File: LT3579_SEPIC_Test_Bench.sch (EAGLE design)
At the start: 159 parts

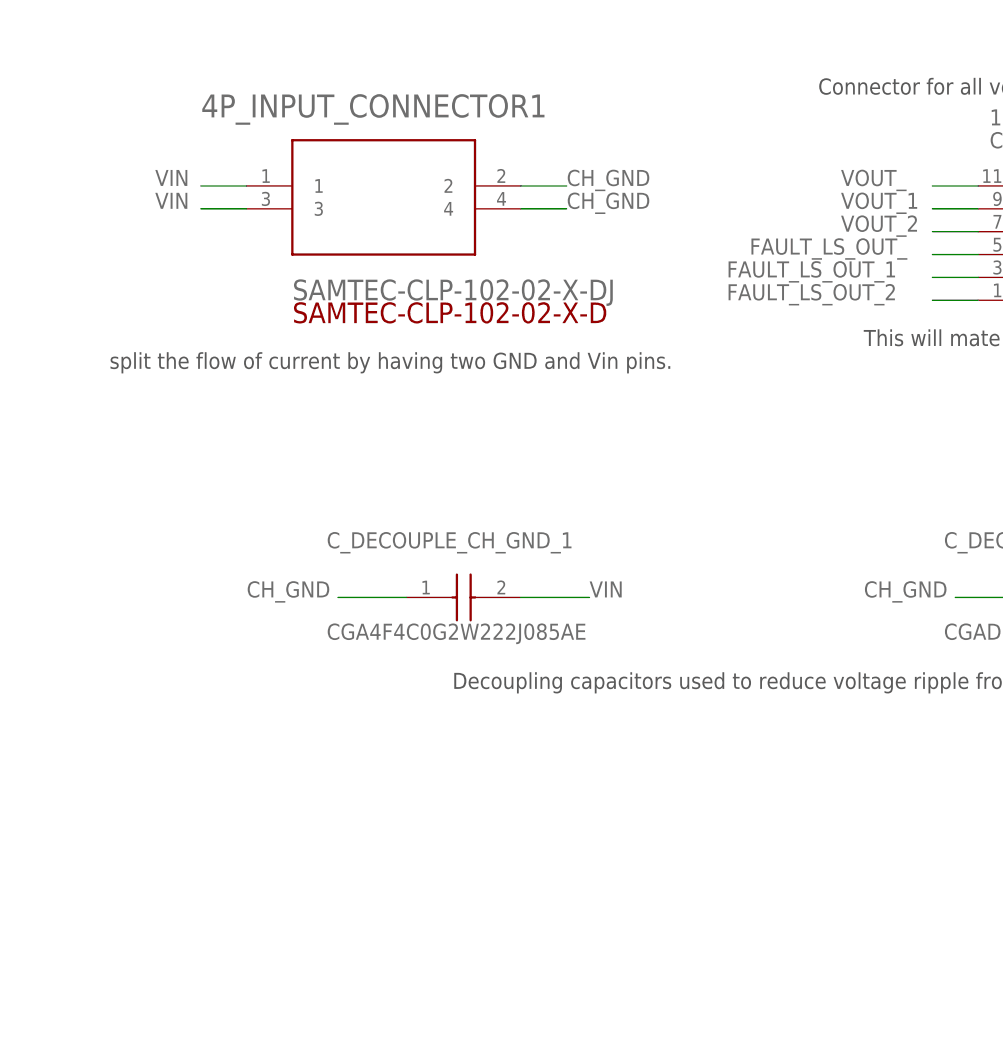
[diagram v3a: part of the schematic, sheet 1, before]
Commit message: Added Reverse Voltage Protection PMOS
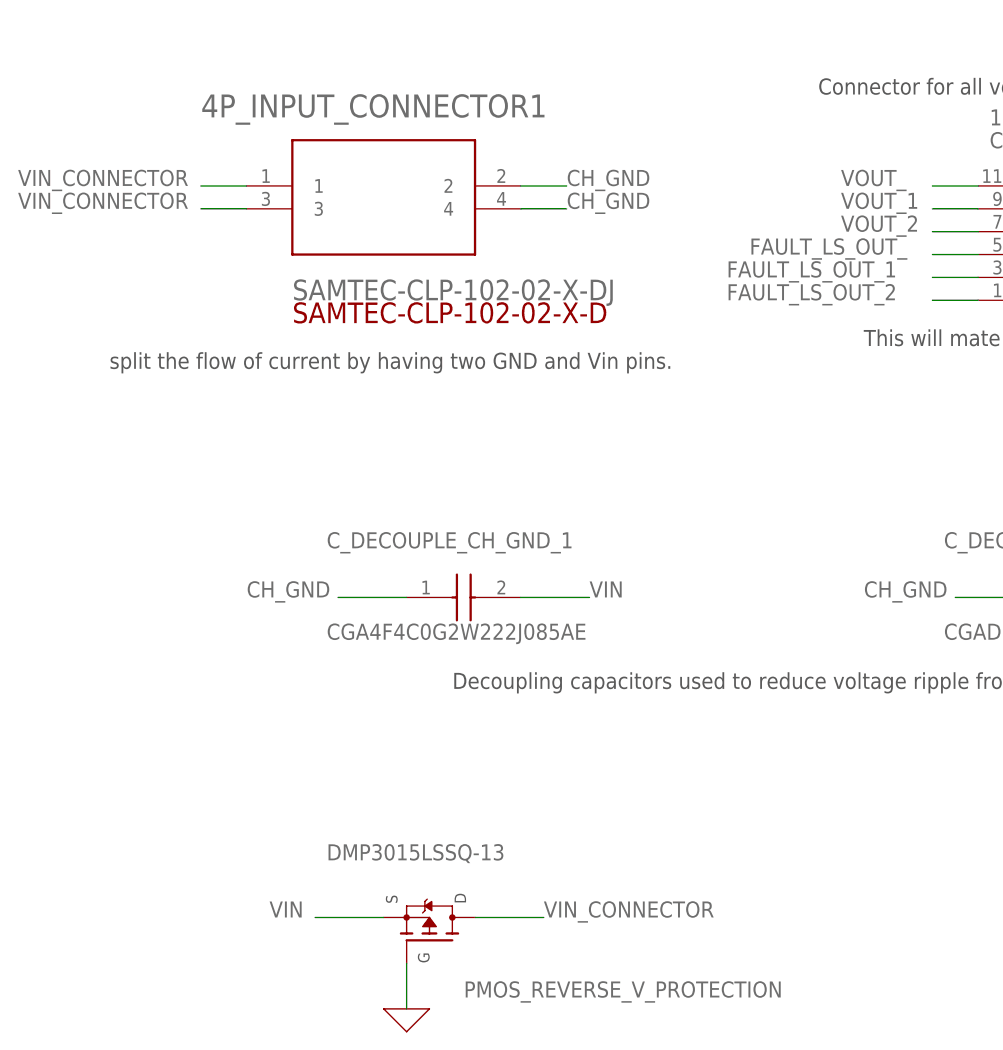
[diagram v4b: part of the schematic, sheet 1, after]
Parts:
- added PMOS_REVERSE_V_PROTECTION: DMP3015LSSQ-13, DMP3015LSSQ-13:DMP3015LSSQ-13
- D1_, D1_1, D1_2: value MBRS360T3G -> MBRS330T3G; device SamacSys_Parts:MBRS360T3G -> SamacSys_Parts:MBRS330T3G
- R_GATE_, R_GATE_1, R_GATE_2: value AC0805DR-0710KL -> AC0805FR-0710KL; device AC0805DR-0710KL:AC0805DR-0710KL -> SamacSys_Parts:AC0805FR-0710KL
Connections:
- new net VIN_CONNECTOR: 4P_INPUT_CONNECTOR1.1, 4P_INPUT_CONNECTOR1.3, PMOS_REVERSE_V_PROTECTION.D1
- net 0: now also PMOS_REVERSE_V_PROTECTION.G1
- net VIN: now also PMOS_REVERSE_V_PROTECTION.S1; no longer 4P_INPUT_CONNECTOR1.1, 4P_INPUT_CONNECTOR1.3
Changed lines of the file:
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@@
 <parts>
 <part name="LT3579_IC_" library="SamacSys_Parts" deviceset="LT3579EFE#PBF" device=""/>
-<part name="D1_" library="SamacSys_Parts" deviceset="MBRS360T3G" device=""/>
+<part name="D1_" library="SamacSys_Parts" deviceset="MBRS330T3G" device=""/>
 <part name="C_IN_1_" library="SamacSys_Parts" deviceset="CGA4J1X7R1E475K125AE" device=""/>
 <part name="C_IN_2_" library="SamacSys_Parts" deviceset="CGA4J1X7R1E475K125AE" device=""/>
@@
 <part name="R_FAULT_" library="AT0805FRE07100KL" deviceset="AT0805FRE07100KL" device=""/>
 <part name="R_FB_" library="AC0805FR-07150KL" deviceset="AC0805FR-07150KL" device=""/>
-<part name="R_GATE_" library="AC0805DR-0710KL" deviceset="AC0805DR-0710KL" device=""/>
+<part name="R_GATE_" library="SamacSys_Parts" deviceset="AC0805FR-0710KL" device=""/>
 <part name="X_3" library="ngspice-simulation" library_urn="urn:adsk.eagle:library:527439" deviceset="GND" device=""/>
 <part name="X_7" library="ngspice-simulation" library_urn="urn:adsk.eagle:library:527439" deviceset="GND" device=""/>
@@
 <part name="TP_D1_" library="S1751-46R" deviceset="S1751-46R" device=""/>
 <part name="LT3579_IC_1" library="SamacSys_Parts" deviceset="LT3579EFE#PBF" device=""/>
-<part name="D1_1" library="SamacSys_Parts" deviceset="MBRS360T3G" device=""/>
+<part name="D1_1" library="SamacSys_Parts" deviceset="MBRS330T3G" device=""/>
 <part name="C_IN_1_1" library="SamacSys_Parts" deviceset="CGA4J1X7R1E475K125AE" device=""/>
 <part name="C_IN_2_1" library="SamacSys_Parts" deviceset="CGA4J1X7R1E475K125AE" device=""/>
@@
 <part name="R_UVLO1_1" library="AC0805FR-0730KL" deviceset="AC0805FR-0730KL" device=""/>
 <part name="R_FAULT_1" library="AT0805FRE07100KL" deviceset="AT0805FRE07100KL" device=""/>
-<part name="R_GATE_1" library="AC0805DR-0710KL" deviceset="AC0805DR-0710KL" device=""/>
+<part name="R_GATE_1" library="SamacSys_Parts" deviceset="AC0805FR-0710KL" device=""/>
 <part name="X_17" library="ngspice-simulation" library_urn="urn:adsk.eagle:library:527439" deviceset="GND" device=""/>
 <part name="X_18" library="ngspice-simulation" library_urn="urn:adsk.eagle:library:527439" deviceset="GND" device=""/>
@@
 <part name="R_FB_1" library="AC0603FR-0764K9L" deviceset="AC0603FR-0764K9L" device=""/>
 <part name="LT3579_IC_2" library="SamacSys_Parts" deviceset="LT3579EFE#PBF" device=""/>
-<part name="D1_2" library="SamacSys_Parts" deviceset="MBRS360T3G" device=""/>
+<part name="D1_2" library="SamacSys_Parts" deviceset="MBRS330T3G" device=""/>
 <part name="C_IN_1_2" library="SamacSys_Parts" deviceset="CGA4J1X7R1E475K125AE" device=""/>
 <part name="C_IN_2_2" library="SamacSys_Parts" deviceset="CGA4J1X7R1E475K125AE" device=""/>
@@
 <part name="R_UVLO1_2" library="AC0805FR-0730KL" deviceset="AC0805FR-0730KL" device=""/>
 <part name="R_FAULT_2" library="AT0805FRE07100KL" deviceset="AT0805FRE07100KL" device=""/>
-<part name="R_GATE_2" library="AC0805DR-0710KL" deviceset="AC0805DR-0710KL" device=""/>
+<part name="R_GATE_2" library="SamacSys_Parts" deviceset="AC0805FR-0710KL" device=""/>
 <part name="X_33" library="ngspice-simulation" library_urn="urn:adsk.eagle:library:527439" deviceset="GND" device=""/>
 <part name="X_34" library="ngspice-simulation" library_urn="urn:adsk.eagle:library:527439" deviceset="GND" device=""/>
@@
 <part name="NMOS_LDO_1" library="SamacSys_Parts" deviceset="RSR025N03HZGTL" device=""/>
 <part name="NMOS_LDO_2" library="SamacSys_Parts" deviceset="RSR025N03HZGTL" device=""/>
+<part name="PMOS_REVERSE_V_PROTECTION" library="DMP3015LSSQ-13" deviceset="DMP3015LSSQ-13" device=""/>
+<part name="X_51" library="ngspice-simulation" library_urn="urn:adsk.eagle:library:527439" deviceset="GND" device=""/>
 </parts>
 <sheets>
@@
 <attribute name="VALUE" x="60.96" y="25.4" size="1.778" layer="96"/>
 </instance>
+<instance part="PMOS_REVERSE_V_PROTECTION" gate="G$1" x="-38.1" y="-55.88" smashed="yes" rot="R90">
+<attribute name="VALUE" x="-49.53" y="-46.99" size="1.778" layer="96"/>
+<attribute name="NAME" x="-34.29" y="-62.23" size="1.778" layer="95"/>
+</instance>
+<instance part="X_51" gate="G$1" x="-40.64" y="-63.5" smashed="yes"/>
 </instances>
 <busses>
@@
 <net name="VIN" class="0">
 <segment>
-<pinref part="4P_INPUT_CONNECTOR1" gate="A" pin="1"/>
-<wire x1="-58.42" y1="27.94" x2="-63.5" y2="27.94" width="0.1524" layer="91"/>
-<label x="-68.58" y="27.94" size="1.778" layer="95"/>
-</segment>
-<segment>
-<pinref part="4P_INPUT_CONNECTOR1" gate="A" pin="3"/>
-<wire x1="-58.42" y1="25.4" x2="-63.5" y2="25.4" width="0.1524" layer="91"/>
-<label x="-68.58" y="25.4" size="1.778" layer="95"/>
-</segment>
-<segment>
 <pinref part="C_DECOUPLE_CH_GND_1" gate="G$1" pin="2"/>
 <wire x1="-27.94" y1="-17.78" x2="-20.32" y2="-17.78" width="0.1524" layer="91"/>
@@
 <label x="48.26" y="-17.78" size="1.778" layer="95"/>
 </segment>
+<segment>
+<pinref part="PMOS_REVERSE_V_PROTECTION" gate="G$1" pin="S1"/>
+<wire x1="-43.18" y1="-53.34" x2="-50.8" y2="-53.34" width="0.1524" layer="91"/>
+<label x="-55.88" y="-53.34" size="1.778" layer="95"/>
+</segment>
 </net>
 <net name="CH_GND" class="0">
@@
 <wire x1="22.86" y1="15.24" x2="17.78" y2="15.24" width="0.1524" layer="91"/>
 <label x="-5.08" y="15.24" size="1.778" layer="95"/>
+</segment>
+</net>
+<net name="0" class="0">
+<segment>
+<pinref part="PMOS_REVERSE_V_PROTECTION" gate="G$1" pin="G1"/>
+<pinref part="X_51" gate="G$1" pin="0"/>
+<wire x1="-40.64" y1="-58.42" x2="-40.64" y2="-63.5" width="0.1524" layer="91"/>
+</segment>
+</net>
+<net name="VIN_CONNECTOR" class="0">
+<segment>
+<pinref part="4P_INPUT_CONNECTOR1" gate="A" pin="1"/>
+<wire x1="-58.42" y1="27.94" x2="-63.5" y2="27.94" width="0.1524" layer="91"/>
+<label x="-83.82" y="27.94" size="1.778" layer="95"/>
+</segment>
+<segment>
+<pinref part="4P_INPUT_CONNECTOR1" gate="A" pin="3"/>
+<wire x1="-58.42" y1="25.4" x2="-63.5" y2="25.4" width="0.1524" layer="91"/>
+<label x="-83.82" y="25.4" size="1.778" layer="95"/>
+</segment>
+<segment>
+<pinref part="PMOS_REVERSE_V_PROTECTION" gate="G$1" pin="D1"/>
+<wire x1="-33.02" y1="-53.34" x2="-25.4" y2="-53.34" width="0.1524" layer="91"/>
+<label x="-25.4" y="-53.34" size="1.778" layer="95"/>
 </segment>
 </net>
@@
 <pinref part="R_GATE_" gate="G$1" pin="1"/>
 <wire x1="7.62" y1="121.92" x2="45.72" y2="121.92" width="0.1524" layer="91"/>
-<wire x1="17.78" y1="106.68" x2="7.62" y2="106.68" width="0.1524" layer="91"/>
+<wire x1="27.94" y1="106.68" x2="7.62" y2="106.68" width="0.1524" layer="91"/>
 <wire x1="7.62" y1="106.68" x2="7.62" y2="121.92" width="0.1524" layer="91"/>
 <pinref part="R_FB_" gate="G$1" pin="1"/>
@@
 <pinref part="R_GATE_" gate="G$1" pin="2"/>
 <pinref part="PMOS_" gate="G$1" pin="G"/>
-<wire x1="38.1" y1="106.68" x2="55.88" y2="106.68" width="0.1524" layer="91"/>
+<wire x1="45.72" y1="106.68" x2="55.88" y2="106.68" width="0.1524" layer="91"/>
 <wire x1="55.88" y1="106.68" x2="55.88" y2="114.3" width="0.1524" layer="91"/>
 <wire x1="55.88" y1="106.68" x2="66.04" y2="106.68" width="0.1524" layer="91"/>
@@
 <pinref part="R_GATE_1" gate="G$1" pin="1"/>
 <wire x1="7.62" y1="124.46" x2="45.72" y2="124.46" width="0.1524" layer="91"/>
-<wire x1="17.78" y1="109.22" x2="7.62" y2="109.22" width="0.1524" layer="91"/>
+<wire x1="27.94" y1="109.22" x2="7.62" y2="109.22" width="0.1524" layer="91"/>
 <wire x1="7.62" y1="109.22" x2="7.62" y2="124.46" width="0.1524" layer="91"/>
 <wire x1="7.62" y1="109.22" x2="7.62" y2="91.44" width="0.1524" layer="91"/>
@@
 <pinref part="R_GATE_1" gate="G$1" pin="2"/>
 <pinref part="PMOS_1" gate="G$1" pin="G"/>
-<wire x1="38.1" y1="109.22" x2="55.88" y2="109.22" width="0.1524" layer="91"/>
+<wire x1="45.72" y1="109.22" x2="55.88" y2="109.22" width="0.1524" layer="91"/>
 <wire x1="55.88" y1="109.22" x2="55.88" y2="116.84" width="0.1524" layer="91"/>
 <wire x1="55.88" y1="109.22" x2="66.04" y2="109.22" width="0.1524" layer="91"/>
@@
 <pinref part="R_GATE_2" gate="G$1" pin="1"/>
 <wire x1="7.62" y1="124.46" x2="45.72" y2="124.46" width="0.1524" layer="91"/>
-<wire x1="17.78" y1="109.22" x2="7.62" y2="109.22" width="0.1524" layer="91"/>
+<wire x1="27.94" y1="109.22" x2="7.62" y2="109.22" width="0.1524" layer="91"/>
 <wire x1="7.62" y1="109.22" x2="7.62" y2="124.46" width="0.1524" layer="91"/>
 <wire x1="7.62" y1="109.22" x2="7.62" y2="91.44" width="0.1524" layer="91"/>
@@
 <pinref part="R_GATE_2" gate="G$1" pin="2"/>
 <pinref part="PMOS_2" gate="G$1" pin="G"/>
-<wire x1="38.1" y1="109.22" x2="55.88" y2="109.22" width="0.1524" layer="91"/>
+<wire x1="45.72" y1="109.22" x2="55.88" y2="109.22" width="0.1524" layer="91"/>
 <wire x1="55.88" y1="109.22" x2="55.88" y2="116.84" width="0.1524" layer="91"/>
 <wire x1="55.88" y1="109.22" x2="66.04" y2="109.22" width="0.1524" layer="91"/>

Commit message: Modified Board
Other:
- note added: "12-Pin connector carrying Power and Signal out of the board. Will mate with a male connector on the board enclosure."
- note added: "Chasis GND is the car frame."
- note added: "Feedback Resistor (R_B) sets the output voltage of the circuit."
- note added: "Filter to convert pulse signal to DC for MCU. Cutoff set at 700Hz. Gain = 1/3."
- note added: "GND test points to be placed near signal and pwr test points."
- note added: "Input"
- note added: "Input Capacitors to reduce ripple voltage from battery."
- note added: "LDO to step down battery voltage to 3.3V for the lofig level shifter"
- note added: "Logic Level Shifter. 13V to 3.3V for MCU."
- note added: "Oscillator Timing Resistor (R_T) sets the operating freqeuncy of LT3579. Operating Frequency is set to 700KHz."
- note added: "Output Capacitors to reduce voltage ripple"
- note added: "PMOS for output disconnect. GATE pin turns off or on the PMOS."
- note added: "PMOS for reverse voltage protection. If battery is plugged in the wrong way."
- note added: "PWR on light indicator."
- note added: "Pull up resistor for the FAULT indicator pin. FAULT can be pulled low externally or internally."
- note added: "R_C,C_C, and C_F form a recictor-capacitor network to compensate the voltage feedback loop in the LT3579."
- note added: "Shunt resistor to measure the difference between chasis GND and signal GND."
- note added: "Soft-start: C_SS is in series w/ integrated 250K resistor of LT3579. Determins the charging and discharing rate when the part shutsdown."
- note added: "Voltage divider by R_UVLO1/2 set the low voltage lockout for the LT3579. UVLO is set at 10V. LT3579 will turn off, if this min threshold is not met to protect battery."
- note removed: "13V FAULT logic level -> 3.3V Logic Level"
- note removed: "Connector for all voltage outputs, GNDs, CLK, and Faults."
- note removed: "Filter to convert pulse signal to DC"
- note removed: "Shunt resistor to measure difference between GNDS."
- note removed: "This will mate with the male connector on the enclosure."
- moved on the sheet: 12P_OUTPUT_CONNECTOR1, 4P_INPUT_CONNECTOR1, C_1_, C_68N_FILTER_, C_68N_FILTER_1, C_68N_FILTER_2, C_C_, C_C_1, C_C_2, C_DECOUPLE_CH_GND_1, C_DECOUPLE_CH_GND_2, C_F_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

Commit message: modified layout
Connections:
- removed net 0: C_68N_FILTER_.2, C_68N_FILTER_1.2, C_68N_FILTER_2.2, C_C_.2, C_C_1.2, C_C_2.2, C_F_.2, C_F_1.2, C_F_2.2, C_IN_1_.2, C_IN_1_1.2, C_IN_1_2.2, C_IN_2_.2, C_IN_2_1.2, C_IN_2_2.2, C_LDO_IN_.2, C_LDO_OUT_.2, C_LS_.2, C_LS_1.2, C_LS_2.2, C_OUT_1_.2, C_OUT_1_1.2, C_OUT_1_2.2, C_OUT_2_.2, C_OUT_2_1.2, C_OUT_2_2.2, C_OUT_3_.2, C_OUT_3_1.2, C_OUT_3_2.2, C_SS_.2, C_SS_1.2, C_SS_2.2, L1L2_.4, L1L2_1.4, L1L2_2.4, LED_.K, LED_1.K, LED_2.K, LT3579_IC_.EPAD, LT3579_IC_1.EPAD, LT3579_IC_2.EPAD, NMOS_LDO_.S, NMOS_LDO_1.S, NMOS_LDO_2.S, PMOS_REVERSE_V_PROTECTION.G1, R_5K_FILTER_\.2, R_5K_FILTER_\1.2, R_5K_FILTER_\2.2, R_T_.2, R_T_1.2, R_T_2.2, R_UVLO2_.1, R_UVLO2_1.1, R_UVLO2_2.1, TP_GND1_.1, TP_GND1_1.1, TP_GND1_2.1, TP_GND2_.1, TP_GND2_1.1, TP_GND2_2.1, TP_GND3_.1, TP_GND3_1.1, TP_GND3_2.1, TP_GND4_.1, TP_GND4_1.1, TP_GND4_2.1
- net CH_GND: now also PMOS_REVERSE_V_PROTECTION.G1
- net GND: now also C_68N_FILTER_.2, C_68N_FILTER_1.2, C_68N_FILTER_2.2, C_C_.2, C_C_1.2, C_C_2.2, C_F_.2, C_F_1.2, C_F_2.2, C_IN_1_.2, C_IN_1_1.2, C_IN_1_2.2, C_IN_2_.2, C_IN_2_1.2, C_IN_2_2.2, C_LDO_IN_.2, C_LDO_OUT_.2, C_LS_.2, C_LS_1.2, C_LS_2.2, C_OUT_1_.2, C_OUT_1_1.2, C_OUT_1_2.2, C_OUT_2_.2, C_OUT_2_1.2, C_OUT_2_2.2, C_OUT_3_.2, C_OUT_3_1.2, C_OUT_3_2.2, C_SS_.2, C_SS_1.2, C_SS_2.2, L1L2_.4, L1L2_1.4, L1L2_2.4, LED_.K, LED_1.K, LED_2.K, LT3579_IC_.EPAD, LT3579_IC_1.EPAD, LT3579_IC_2.EPAD, NMOS_LDO_.S, NMOS_LDO_1.S, NMOS_LDO_2.S, R_5K_FILTER_\.2, R_5K_FILTER_\1.2, R_5K_FILTER_\2.2, R_T_.2, R_T_1.2, R_T_2.2, R_UVLO2_.1, R_UVLO2_1.1, R_UVLO2_2.1, TP_GND1_.1, TP_GND1_1.1, TP_GND1_2.1, TP_GND2_.1, TP_GND2_1.1, TP_GND2_2.1, TP_GND3_.1, TP_GND3_1.1, TP_GND3_2.1, TP_GND4_.1, TP_GND4_1.1, TP_GND4_2.1
